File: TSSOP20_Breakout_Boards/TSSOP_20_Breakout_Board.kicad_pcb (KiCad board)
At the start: 2 copper layers, 27 x 32 mm, 6 parts, among them J1 Conn_01x10, J2 Conn_01x10, J3 Conn_01x01, J4 Conn_01x01

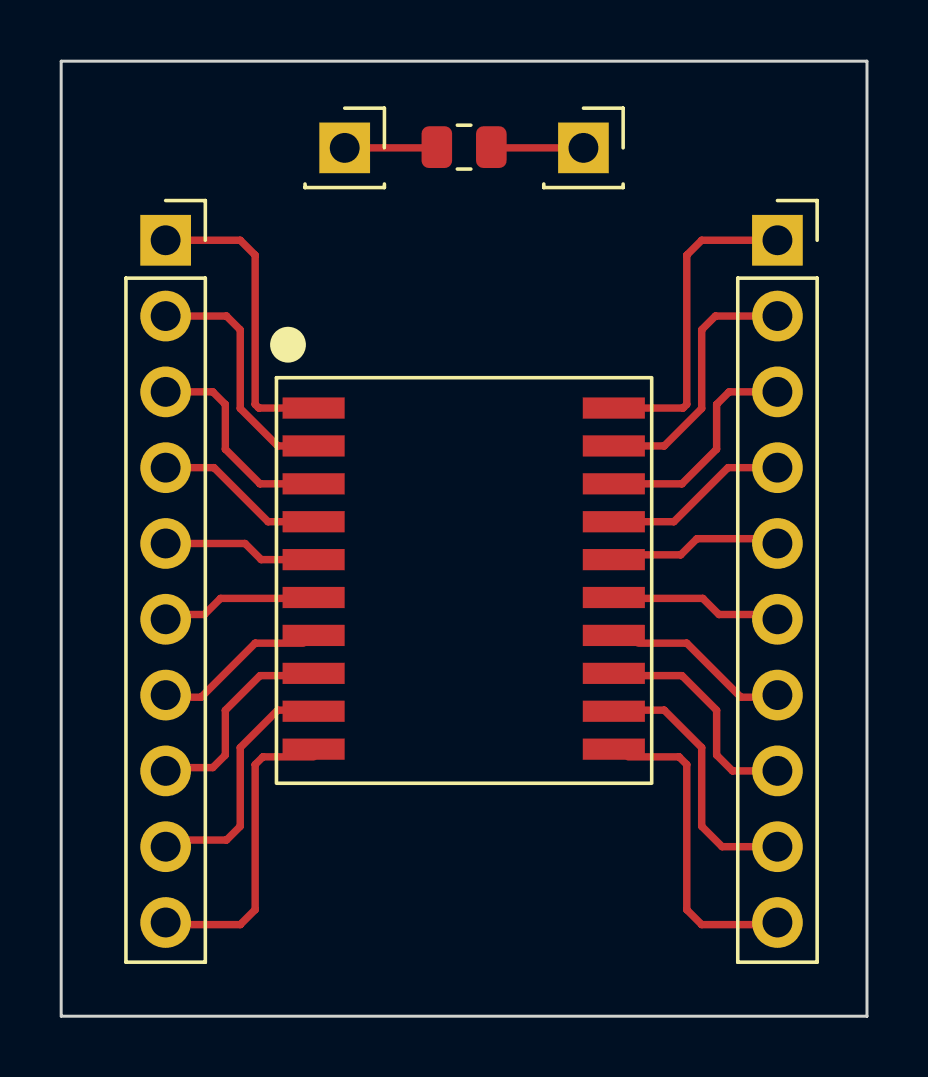
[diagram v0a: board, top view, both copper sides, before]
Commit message: finalized tssop 20 design
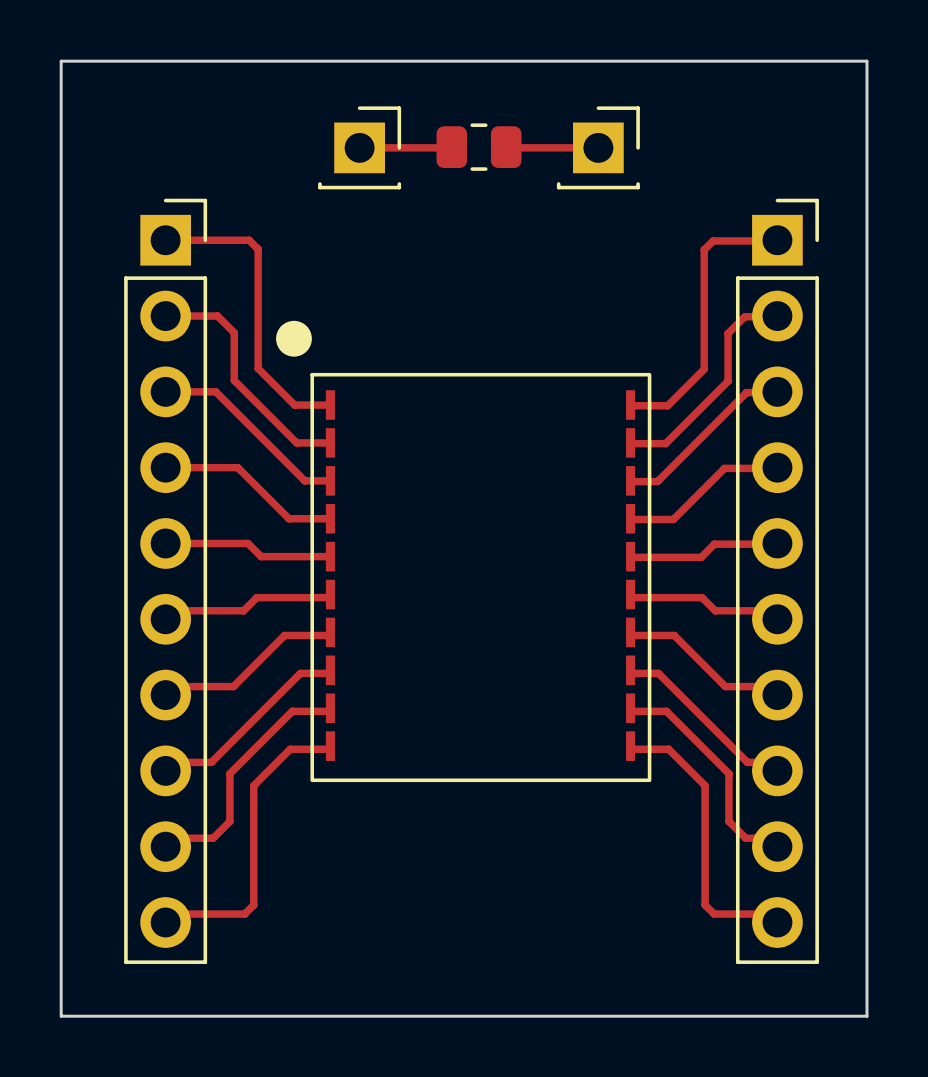
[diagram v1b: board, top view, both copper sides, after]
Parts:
- removed SOIC20: 20_Pin_SOIC_Board, SOIC_Footprints:20_Pin_SOIC_Board
- added TSSOP20: 20_Pin_TSSOP_Board, TSSOP_Footprints:20_Pin_TSSOP_Board, F.Cu at (156.0, 105.8)
- moved J3 0.50 mm to (160.0, 91.4)
- moved J4 0.50 mm to (152.0, 91.4)
- moved R1 0.50 mm to (156.0, 91.4)
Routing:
- net Net-(J2-Pad6): track 5.18 -> 5.70 mm
- net Net-(J1-Pad6): track 5.18 -> 5.70 mm
- net Net-(J1-Pad5): track 5.18 -> 5.70 mm
- net Net-(J2-Pad7): track 5.71 -> 6.23 mm
- net Net-(J2-Pad4): track 5.71 -> 6.23 mm
- net Net-(J1-Pad7): track 5.71 -> 6.23 mm
- net Net-(J1-Pad4): track 5.71 -> 6.23 mm
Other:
- board text added: "20 Pin TSSOP Breakout Board"
- board text removed: "20 Pin SOIC Breakout Board"
